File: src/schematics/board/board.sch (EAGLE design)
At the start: 12 parts, among them Q1 12MHz, U1 MCP17003302E/TO, U2 PIC18F14K50-E-P, X1 PN61729-S

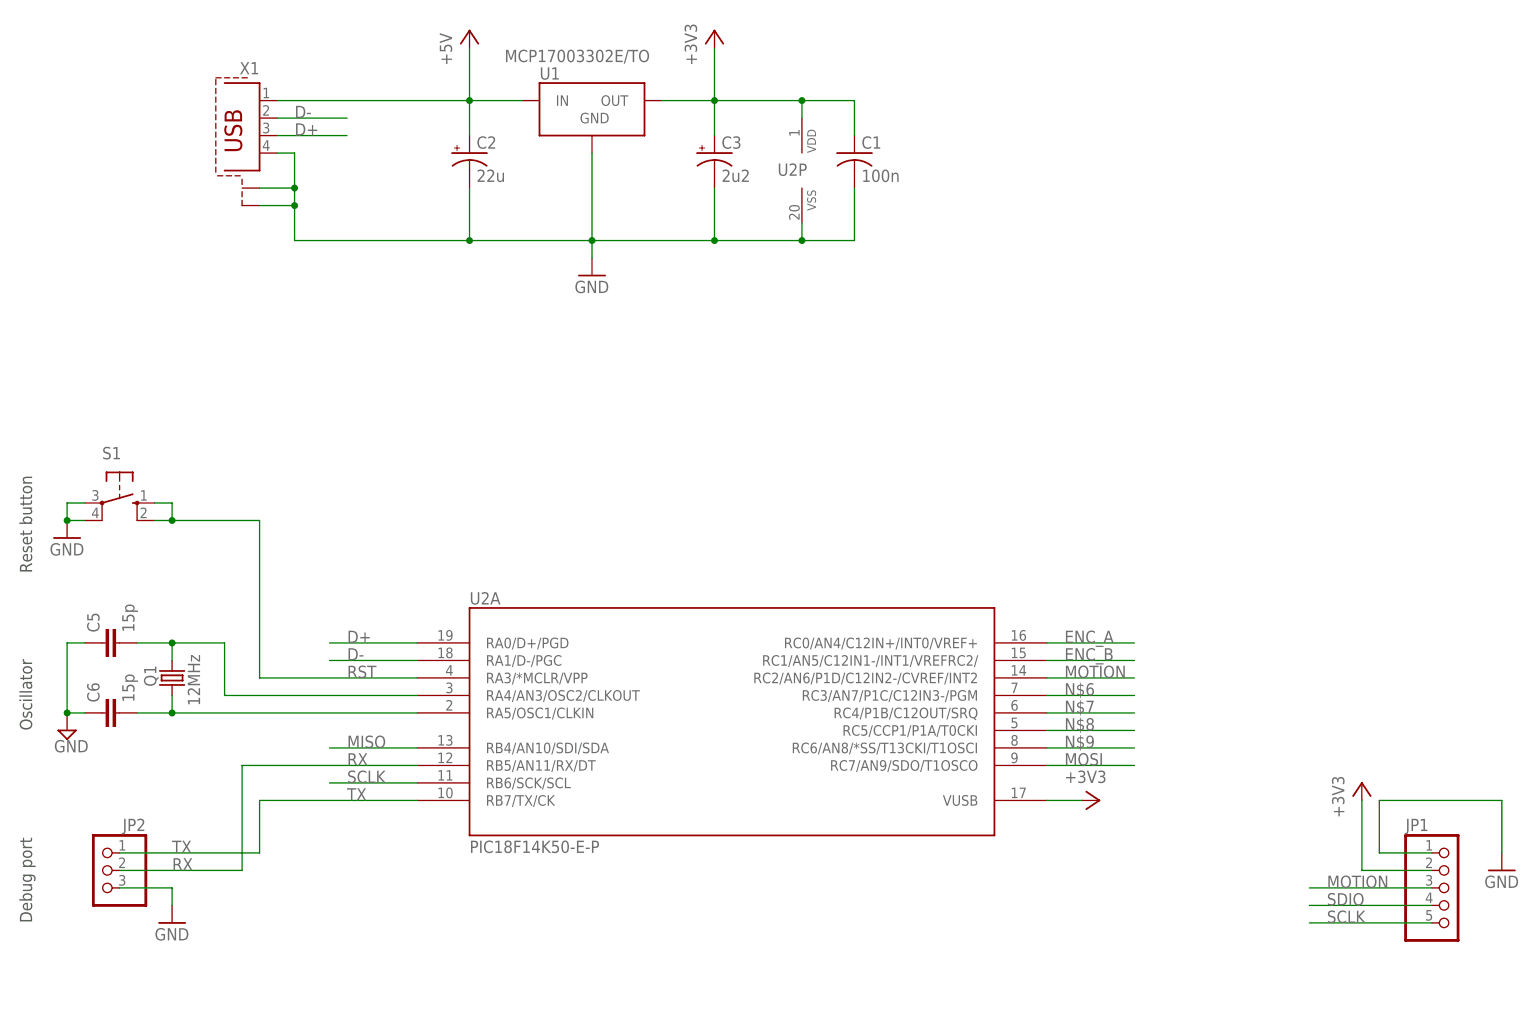
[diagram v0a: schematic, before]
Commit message: Main board PCB draft
Added a draft of the main board PCB.

Andrea Zoppi
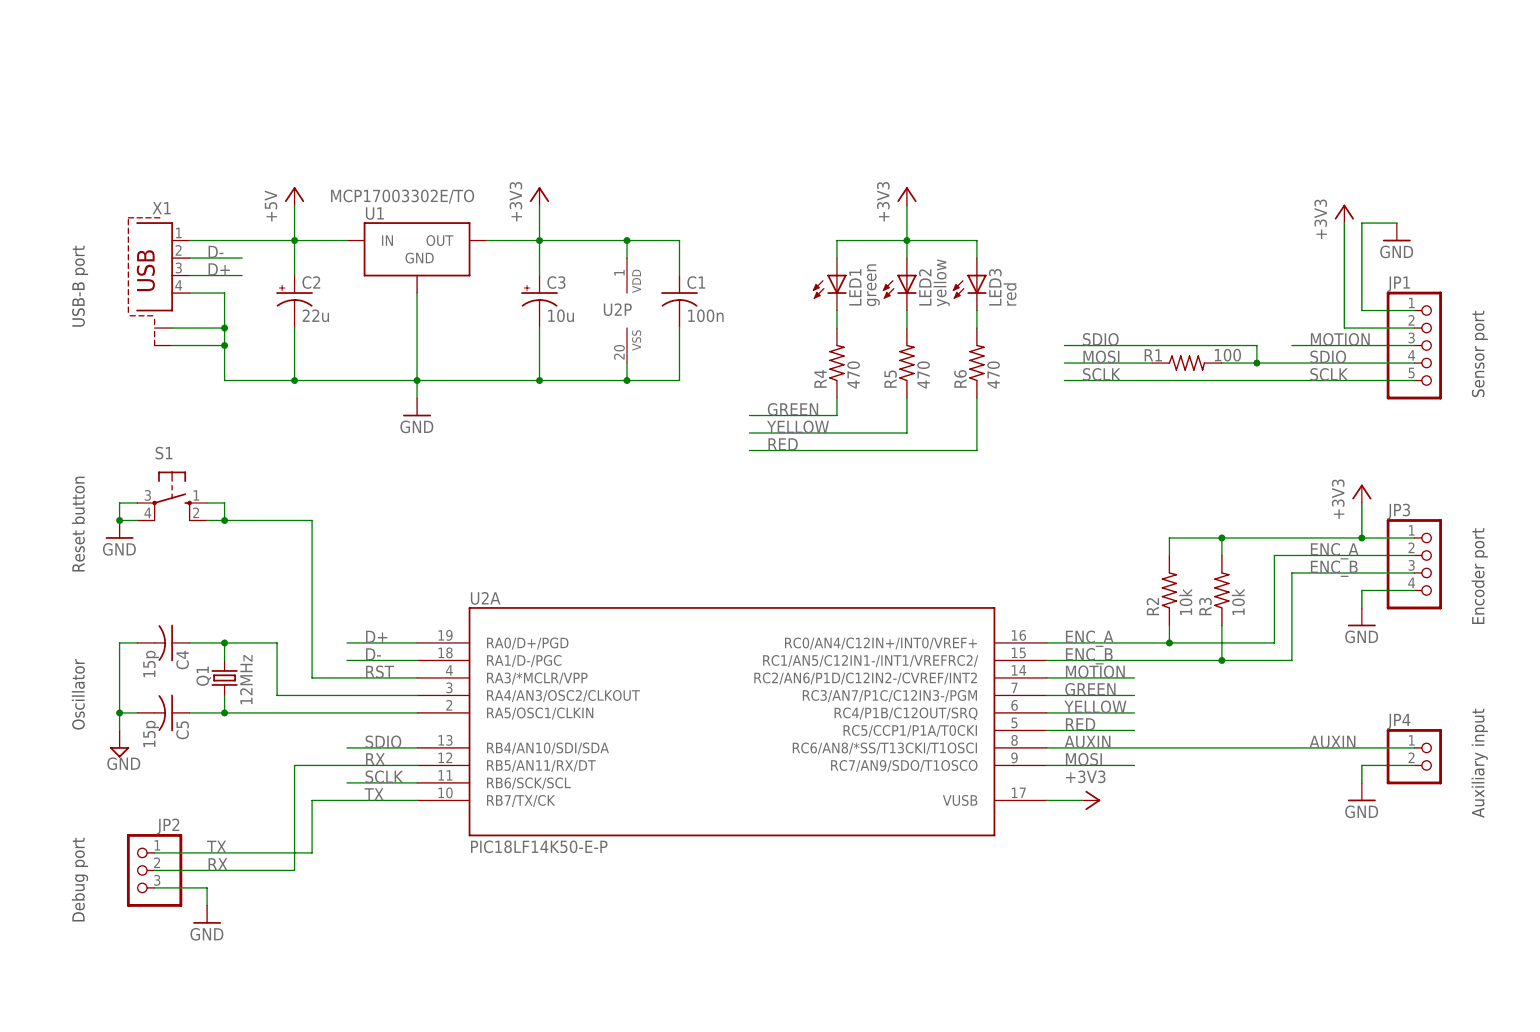
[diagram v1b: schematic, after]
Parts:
- removed C6: 15p, resistor:C-EU025-025X050
- added C4: 15p, rcl:C-US025-025X050
- added JP3: (no value), pinhead:PINHD-1X4
- added JP4: (no value), pinhead:PINHD-1X2
- added LED1: green, led:LED3MM
- added LED2: yellow, led:LED3MM
- added LED3: red, led:LED3MM
- added R1: 100, rcl:R-US_0207/10
- added R2, R3: 10k, rcl:R-US_0204/5
- added R4, R5, R6: 470, rcl:R-US_0204/5
- C2: device rcl:CPOL-USE5-6 -> rcl:CPOL-USE2-5
- C3: value 2u2 -> 10u; device rcl:CPOL-USE2.5-5 -> rcl:CPOL-USE2-5
- C5: device resistor:C-EU025-025X050 -> rcl:C-US025-025X050
- U2: value PIC18F14K50-E-P -> PIC18LF14K50-E-P
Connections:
- removed net MISO: U2A.RB4/AN10/SDI/SDA
- removed net N$8: U2A.RC5/CCP1/P1A/T0CKI
- removed net N$9: U2A.RC6/AN8/*SS/T13CKI/T1OSCI
- new net AUXIN: JP4.1, U2A.RC6/AN8/*SS/T13CKI/T1OSCI
- new net GREEN: R4.1, U2A.RC3/AN7/P1C/C12IN3-/PGM
- new net N$5: LED1.C, R4.2
- new net RED: R6.1, U2A.RC5/CCP1/P1A/T0CKI
- new net YELLOW: R5.1, U2A.RC4/P1B/C12OUT/SRQ
- net +3V3: now also JP3.1, LED1.A, LED2.A, LED3.A, R2.2, R3.2
- net ENC_A: now also JP3.2, R2.1
- net ENC_B: now also JP3.3, R3.1
- net GND: now also C4.2, C5.2, JP3.4, JP4.2; no longer C5.1, C6.1
- net MOSI: now also R1.1
- net N$2: now also C4.1; no longer C5.2
- net N$3: now also C5.1; no longer C6.2
- net N$6: now also LED2.C, R5.2; no longer U2A.RC3/AN7/P1C/C12IN3-/PGM
- net N$7: now also LED3.C, R6.2; no longer U2A.RC4/P1B/C12OUT/SRQ
- net SDIO: now also R1.2, U2A.RB4/AN10/SDI/SDA
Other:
- note added: "Auxiliary input"
- note added: "Encoder port"
- note added: "Sensor port"
- note added: "USB-B port"
- moved on the sheet: C1, C2, C3, C5, JP1, JP2, Q1, S1, U1, U2P, X1

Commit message: PCBs updated
Minor changes were done to both the main board and sensor module PCB
layouts.

Andrea Zoppi
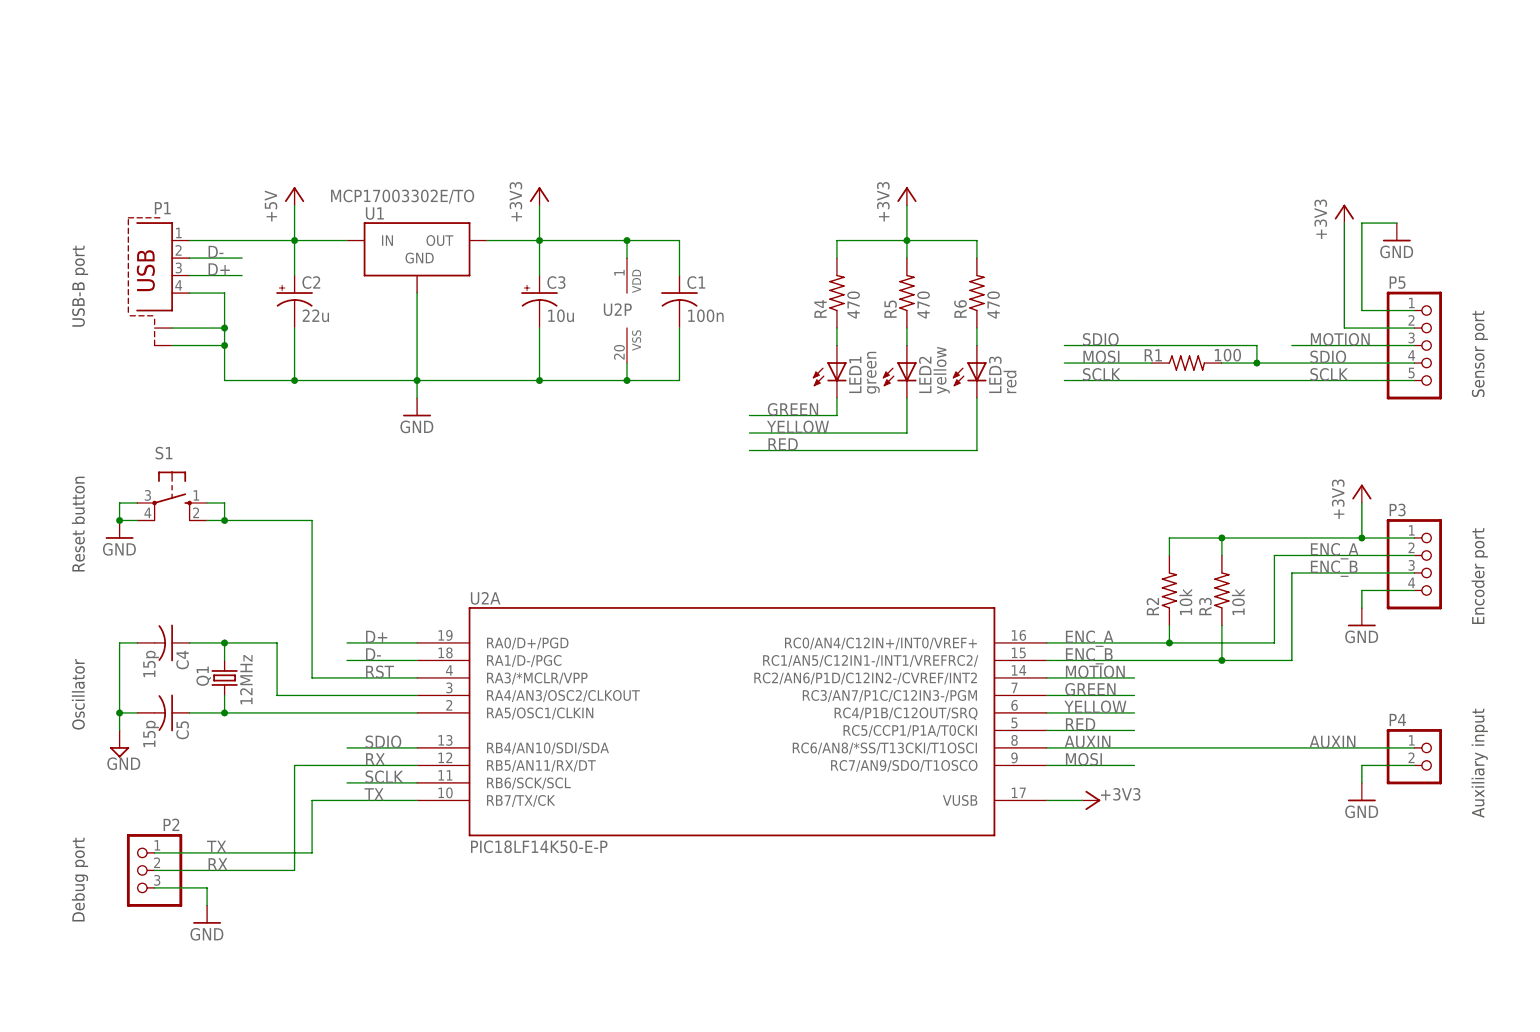
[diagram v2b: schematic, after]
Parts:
- renumbered JP1 to P5, JP2 to P2, JP3 to P3, JP4 to P4, X1 to P1
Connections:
- removed net N$6: LED2.C, R5.2
- removed net N$7: LED3.C, R6.2
- new net N$1: LED3.A, R6.1
- new net N$4: LED2.A, R5.1
- net +3V3: now also R4.2, R5.2, R6.2; no longer LED1.A, LED2.A, LED3.A
- net GREEN: now also LED1.C; no longer R4.1
- net N$5: now also LED1.A, R4.1; no longer LED1.C, R4.2
- net RED: now also LED3.C; no longer R6.1
- net YELLOW: now also LED2.C; no longer R5.1
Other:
- moved on the sheet: LED1, LED2, LED3, R4, R5, R6

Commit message: Added UART pull-ups
Added pull-ups to the UART port, so that there are never mistaken signals.
They are not critical, but may help in keeping consistent values,
especially for the receiver.

Andrea Zoppi
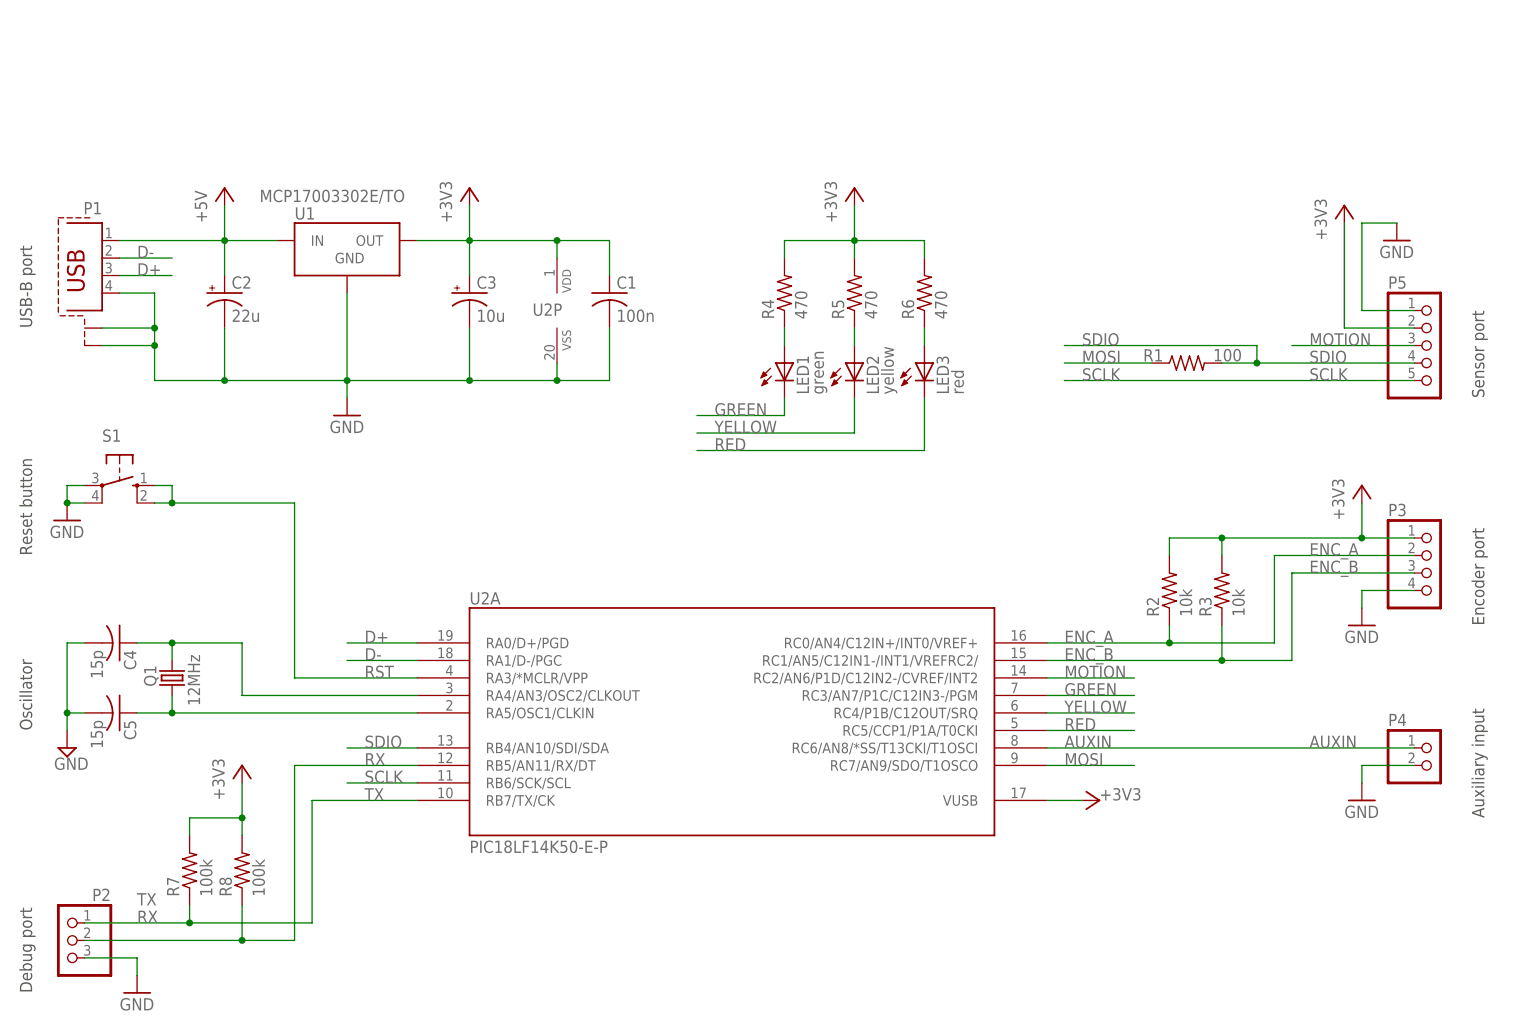
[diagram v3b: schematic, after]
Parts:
- added R7, R8: 100k, rcl:R-US_0204/5
- C1: device rcl:C-US050-025X075 -> rcl:C-US025-025X050
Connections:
- net +3V3: now also R7.2, R8.2
- net RX: now also R8.1
- net TX: now also R7.1
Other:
- moved on the sheet: C1, C2, C3, C4, C5, LED1, LED2, LED3, P1, P2, Q1, R4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

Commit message: Added user button pull-up
A pull-up resistor was added to the user button, because the built-in weak
pull-up of the MCU does not work properly at power-up.

Andrea Zoppi
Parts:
- added R9: 47k, rcl:R-US_0204/5
- R7, R8: value 100k -> 47k
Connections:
- net +3V3: now also R9.2
- net RST: now also R9.1
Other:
- moved on the sheet: S1
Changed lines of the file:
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@@
 <part name="P4" library="pinhead" deviceset="PINHD-1X2" device=""/>
 <part name="GND6" library="supply1" deviceset="GND" device=""/>
-<part name="R7" library="rcl" deviceset="R-US_" device="0204/5" value="100k"/>
-<part name="R8" library="rcl" deviceset="R-US_" device="0204/5" value="100k"/>
+<part name="R7" library="rcl" deviceset="R-US_" device="0204/5" value="47k"/>
+<part name="R8" library="rcl" deviceset="R-US_" device="0204/5" value="47k"/>
 <part name="+3V6" library="supply1" deviceset="+3V3" device=""/>
+<part name="+3V7" library="supply1" deviceset="+3V3" device=""/>
+<part name="R9" library="rcl" deviceset="R-US_" device="0204/5" value="47k"/>
 </parts>
 <sheets>
@@
 </instance>
 <instance part="SUPPLY1" gate="GND" x="-17.78" y="2.54"/>
-<instance part="S1" gate="1" x="-10.16" y="40.64" rot="R270"/>
+<instance part="S1" gate="1" x="-10.16" y="33.02" rot="R270"/>
 <instance part="P2" gate="A" x="-17.78" y="-25.4" rot="MR0"/>
-<instance part="GND3" gate="1" x="-17.78" y="35.56"/>
+<instance part="GND3" gate="1" x="-17.78" y="27.94"/>
 <instance part="GND4" gate="1" x="-7.62" y="-33.02"/>
 <instance part="+3V2" gate="G$1" x="132.08" y="-5.08" smashed="yes" rot="R270">
@@
 <instance part="R8" gate="G$1" x="7.62" y="-15.24" rot="R90"/>
 <instance part="+3V6" gate="G$1" x="7.62" y="0"/>
+<instance part="+3V7" gate="G$1" x="15.24" y="48.26"/>
+<instance part="R9" gate="G$1" x="15.24" y="38.1" rot="R90"/>
 </instances>
 <busses>
@@
 </segment>
 <segment>
-<wire x1="-17.78" y1="38.1" x2="-15.24" y2="38.1" width="0.1524" layer="91"/>
-<wire x1="-15.24" y1="40.64" x2="-17.78" y2="40.64" width="0.1524" layer="91"/>
-<wire x1="-17.78" y1="40.64" x2="-17.78" y2="38.1" width="0.1524" layer="91"/>
-<junction x="-17.78" y="38.1"/>
+<wire x1="-17.78" y1="30.48" x2="-15.24" y2="30.48" width="0.1524" layer="91"/>
+<wire x1="-15.24" y1="33.02" x2="-17.78" y2="33.02" width="0.1524" layer="91"/>
+<wire x1="-17.78" y1="33.02" x2="-17.78" y2="30.48" width="0.1524" layer="91"/>
+<junction x="-17.78" y="30.48"/>
 <pinref part="S1" gate="1" pin="P1"/>
 <pinref part="S1" gate="1" pin="P"/>
@@
 <junction x="7.62" y="-7.62"/>
 </segment>
+<segment>
+<pinref part="+3V7" gate="G$1" pin="+3V3"/>
+<pinref part="R9" gate="G$1" pin="2"/>
+<wire x1="15.24" y1="45.72" x2="15.24" y2="43.18" width="0.1524" layer="91"/>
+</segment>
 </net>
 <net name="N$2" class="0">
@@
 <net name="RST" class="0">
 <segment>
-<wire x1="15.24" y1="38.1" x2="-2.54" y2="38.1" width="0.1524" layer="91"/>
-<wire x1="-2.54" y1="38.1" x2="-5.08" y2="38.1" width="0.1524" layer="91"/>
-<wire x1="-5.08" y1="40.64" x2="-2.54" y2="40.64" width="0.1524" layer="91"/>
-<wire x1="-2.54" y1="40.64" x2="-2.54" y2="38.1" width="0.1524" layer="91"/>
-<junction x="-2.54" y="38.1"/>
+<wire x1="15.24" y1="30.48" x2="-2.54" y2="30.48" width="0.1524" layer="91"/>
+<wire x1="-2.54" y1="30.48" x2="-5.08" y2="30.48" width="0.1524" layer="91"/>
+<wire x1="-5.08" y1="33.02" x2="-2.54" y2="33.02" width="0.1524" layer="91"/>
+<wire x1="-2.54" y1="33.02" x2="-2.54" y2="30.48" width="0.1524" layer="91"/>
+<junction x="-2.54" y="30.48"/>
 <pinref part="S1" gate="1" pin="S1"/>
 <pinref part="S1" gate="1" pin="S"/>
-<wire x1="15.24" y1="38.1" x2="15.24" y2="12.7" width="0.1524" layer="91"/>
+<wire x1="15.24" y1="30.48" x2="15.24" y2="12.7" width="0.1524" layer="91"/>
 <pinref part="U2" gate="A" pin="RA3/*MCLR/VPP"/>
 <wire x1="15.24" y1="12.7" x2="33.02" y2="12.7" width="0.1524" layer="91"/>
 <label x="25.4" y="12.7" size="1.778" layer="95"/>
-</segment>
-</net>
+<pinref part="R9" gate="G$1" pin="1"/>
+<wire x1="15.24" y1="33.02" x2="15.24" y2="30.48" width="0.1524" layer="91"/>
+<junction x="15.24" y="30.48"/>
+</segment>
+</net>

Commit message: Minor PCB fixes
Changed resistor values so that performance is improved, and the PIC
inputs can read correct pull-up values.

Andrea Zoppi
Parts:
- C2: value 22u -> 2u2
- R1: value 100 -> 150
- R7, R8, R9: value 47k -> 100k
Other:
- note added: "LEDs"
- note added: "Power stage"
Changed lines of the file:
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@@
 <part name="GND1" library="supply1" deviceset="GND" device=""/>
 <part name="C1" library="rcl" deviceset="C-US" device="025-025X050" value="100n"/>
-<part name="C2" library="rcl" deviceset="CPOL-US" device="E2-5" value="22u"/>
+<part name="C2" library="rcl" deviceset="CPOL-US" device="E2-5" value="2u2"/>
 <part name="C3" library="rcl" deviceset="CPOL-US" device="E2-5" value="10u"/>
 <part name="Q1" library="crystal" deviceset="CRYSTAL" device="HC49S" value="12MHz"/>
@@
 <part name="C4" library="rcl" deviceset="C-US" device="025-025X050" value="15p"/>
 <part name="C5" library="rcl" deviceset="C-US" device="025-025X050" value="15p"/>
-<part name="R1" library="rcl" deviceset="R-US_" device="0207/10" value="100"/>
+<part name="R1" library="rcl" deviceset="R-US_" device="0207/10" value="150"/>
 <part name="R2" library="rcl" deviceset="R-US_" device="0204/5" value="10k"/>
 <part name="R3" library="rcl" deviceset="R-US_" device="0204/5" value="10k"/>
@@
 <part name="P4" library="pinhead" deviceset="PINHD-1X2" device=""/>
 <part name="GND6" library="supply1" deviceset="GND" device=""/>
-<part name="R7" library="rcl" deviceset="R-US_" device="0204/5" value="47k"/>
-<part name="R8" library="rcl" deviceset="R-US_" device="0204/5" value="47k"/>
+<part name="R7" library="rcl" deviceset="R-US_" device="0204/5" value="100k"/>
+<part name="R8" library="rcl" deviceset="R-US_" device="0204/5" value="100k"/>
 <part name="+3V6" library="supply1" deviceset="+3V3" device=""/>
 <part name="+3V7" library="supply1" deviceset="+3V3" device=""/>
-<part name="R9" library="rcl" deviceset="R-US_" device="0204/5" value="47k"/>
+<part name="R9" library="rcl" deviceset="R-US_" device="0204/5" value="100k"/>
 </parts>
 <sheets>
@@
 <text x="187.96" y="-7.62" size="1.778" layer="97" rot="R90">Auxiliary input</text>
 <text x="187.96" y="53.34" size="1.778" layer="97" rot="R90">Sensor port</text>
+<text x="15.24" y="88.9" size="1.778" layer="97">Power stage</text>
+<text x="91.44" y="88.9" size="1.778" layer="97">LEDs</text>
 </plain>
 <instances>
@@
 <segment>
 <wire x1="17.78" y1="-22.86" x2="0" y2="-22.86" width="0.1524" layer="91"/>
-<label x="-7.62" y="-20.32" size="1.778" layer="95"/>
+<label x="-7.62" y="-22.86" size="1.778" layer="95"/>
 <pinref part="P2" gate="A" pin="1"/>
 <pinref part="U2" gate="A" pin="RB7/TX/CK"/>
@@
 <segment>
 <wire x1="15.24" y1="-25.4" x2="7.62" y2="-25.4" width="0.1524" layer="91"/>
-<label x="-7.62" y="-22.86" size="1.778" layer="95"/>
+<label x="-7.62" y="-25.4" size="1.778" layer="95"/>
 <pinref part="P2" gate="A" pin="2"/>
 <pinref part="U2" gate="A" pin="RB5/AN11/RX/DT"/>
